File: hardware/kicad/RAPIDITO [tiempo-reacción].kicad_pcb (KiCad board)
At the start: 2 copper layers, 109.4 x 93.2 mm, 33 parts, among them J2 Screw_Terminal_01x19, J3 Screw_Terminal_01x19, Q1 2N3904

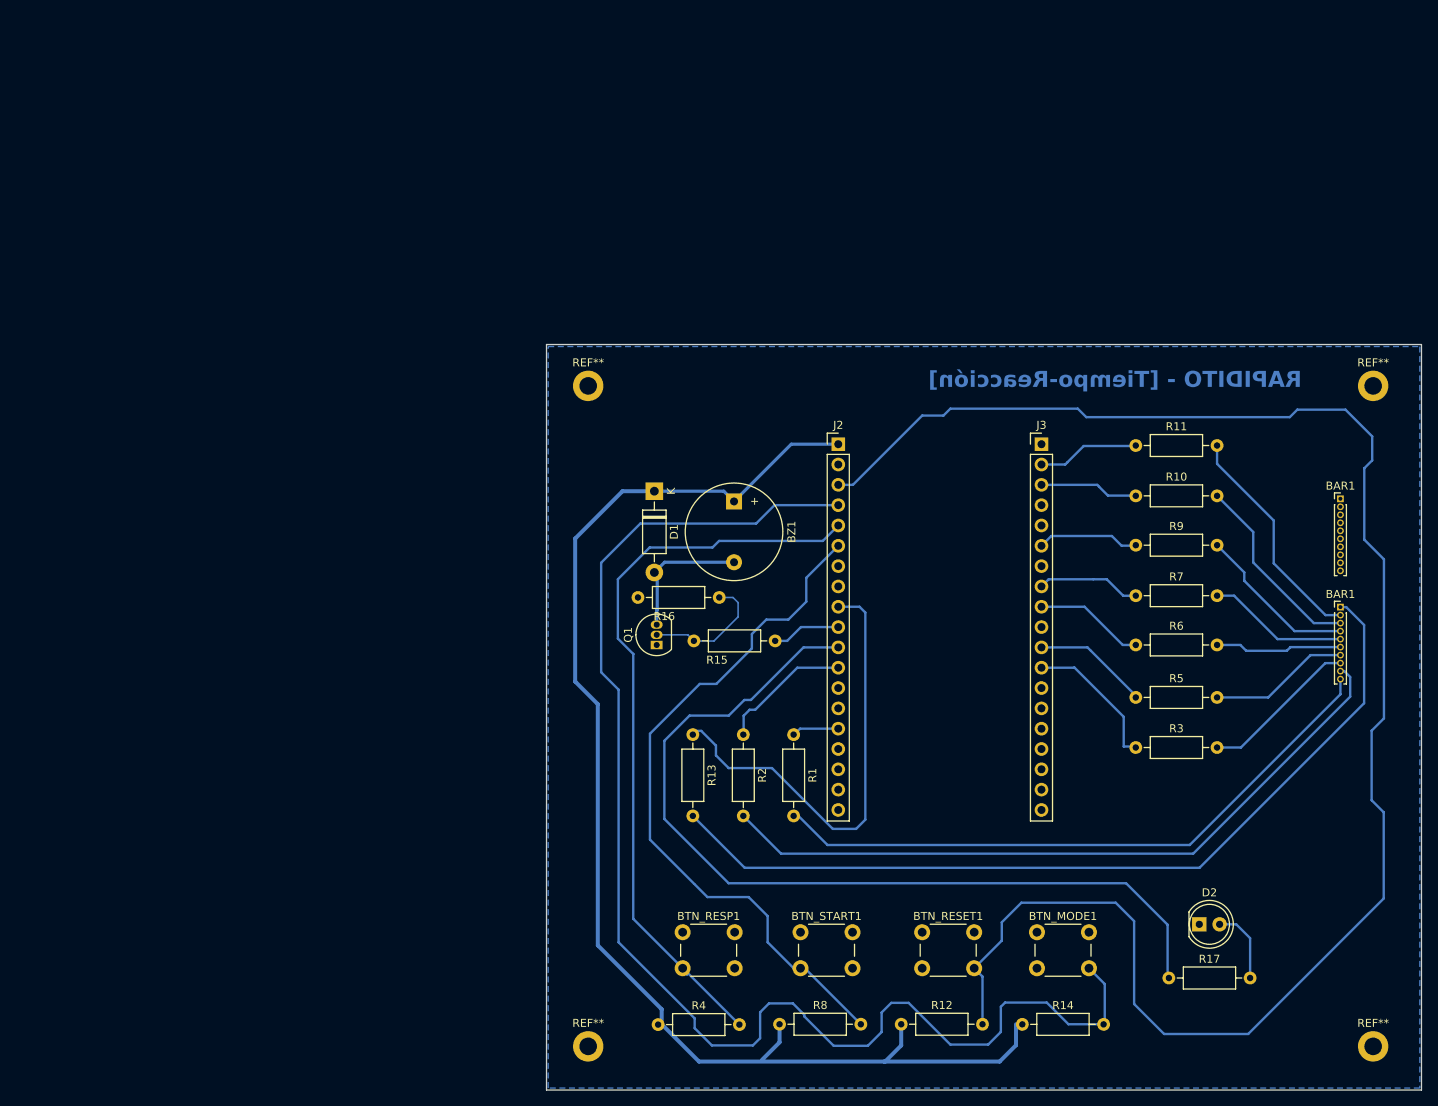
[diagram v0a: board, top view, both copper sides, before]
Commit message: KiCad v0.2: pinout ESP32 DevKit 30 pines, botones con pull-up interna, buzzer a 5 V, resistencias SMD, logo
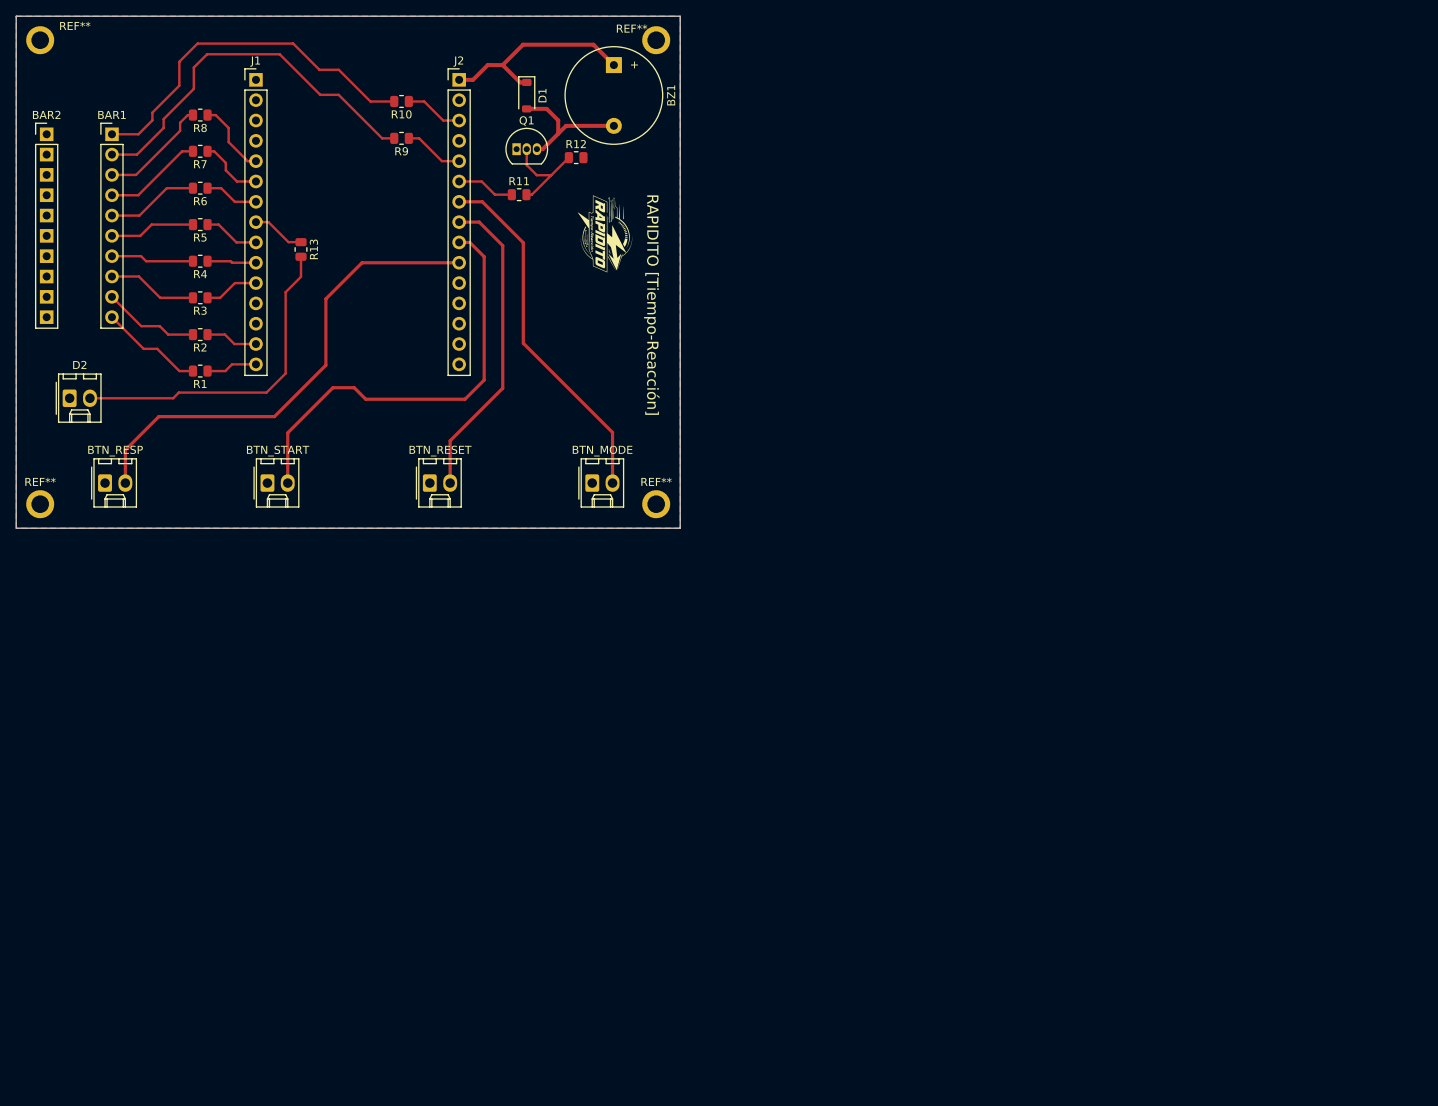
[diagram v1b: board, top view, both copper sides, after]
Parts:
- removed the BAR1 at (165.5, 73.9)
- removed the BAR1 at (165.5, 60.3)
- removed BTN_MODE1: PB4, Button_Switch_THT:SW_PUSH_6mm
- removed BTN_RESET1: PB3, Button_Switch_THT:SW_PUSH_6mm
- removed BTN_RESP1: PB1, Button_Switch_THT:SW_PUSH_6mm
- removed BTN_START1: PB2, Button_Switch_THT:SW_PUSH_6mm
- removed J3: Screw_Terminal_01x19, Connector_PinHeader_2.54mm:PinHeader_1x19_P2.54mm_Vertical
- removed R14, R16: 10kΩ, Resistor_THT:R_Axial_DIN0207_L6.3mm_D2.5mm_P10.16mm_Horizontal
- removed R15: 1kΩ, Resistor_THT:R_Axial_DIN0207_L6.3mm_D2.5mm_P10.16mm_Horizontal
- removed R17: 330Ω, Resistor_THT:R_Axial_DIN0207_L6.3mm_D2.5mm_P10.16mm_Horizontal
- removed the REF** at (169.6, 128.8)
- removed the REF** at (71.5, 128.8)
- removed the REF** at (71.5, 46.2)
- removed the REF** at (169.6, 46.2)
- added BAR1: HDSP-4830_2, Connector_PinHeader_2.54mm:PinHeader_1x10_P2.54mm_Vertical, F.Cu at (12.0, 14.8)
- added BAR2: HDSP-4830_2, Connector_PinHeader_2.54mm:PinHeader_1x10_P2.54mm_Vertical, F.Cu at (3.81, 14.8)
- added BTN_MODE: PB4, Connector_Molex:Molex_KK-254_AE-6410-02A_1x02_P2.54mm_Vertical, F.Cu at (72.0, 58.4)
- added BTN_RESET: PB3, Connector_Molex:Molex_KK-254_AE-6410-02A_1x02_P2.54mm_Vertical, F.Cu at (51.7, 58.4)
- added BTN_RESP: PB1, Connector_Molex:Molex_KK-254_AE-6410-02A_1x02_P2.54mm_Vertical, F.Cu at (11.1, 58.4)
- added BTN_START: PB2, Connector_Molex:Molex_KK-254_AE-6410-02A_1x02_P2.54mm_Vertical, F.Cu at (31.4, 58.4)
- added G***: LOGO, Logo RAPIDITO [tiempo-reacción]:Logo Rapidito negativo 85, F.Cu at (73.6, 27.2)
- added J1: Screw_Terminal_01x15, Connector_PinHeader_2.54mm:PinHeader_1x15_P2.54mm_Vertical, F.Cu at (30.0, 7.96)
- added REF**: MountingHole_2.2mm_M2_ISO7380_Pad, MountingHole:MountingHole_2.2mm_M2_ISO7380_Pad, F.Cu at (3.00, 61.0)
- added REF**: MountingHole_2.2mm_M2_ISO7380_Pad, MountingHole:MountingHole_2.2mm_M2_ISO7380_Pad, F.Cu at (80.0, 61.0)
- added REF**: MountingHole_2.2mm_M2_ISO7380_Pad, MountingHole:MountingHole_2.2mm_M2_ISO7380_Pad, F.Cu at (3.00, 3.00)
- added REF**: MountingHole_2.2mm_M2_ISO7380_Pad, MountingHole:MountingHole_2.2mm_M2_ISO7380_Pad, F.Cu at (80.0, 3.00)
- D1: footprint Diode_THT:D_DO-41_SOD81_P10.16mm_Horizontal -> Diode_SMD:D_SOD-123
- D2: footprint LED_THT:LED_D5.0mm -> Connector_Molex:Molex_KK-254_AE-6410-02A_1x02_P2.54mm_Vertical
- J2: value Screw_Terminal_01x19 -> Screw_Terminal_01x15; footprint Connector_PinHeader_2.54mm:PinHeader_1x19_P2.54mm_Vertical -> Connector_PinHeader_2.54mm:PinHeader_1x15_P2.54mm_Vertical
- R1, R10, R12, R13, R2, R3, R5, R6, R7, R9: footprint Resistor_THT:R_Axial_DIN0207_L6.3mm_D2.5mm_P10.16mm_Horizontal -> Resistor_SMD:R_0805_2012Metric
- R11: value 330Ω -> 1kΩ; footprint Resistor_THT:R_Axial_DIN0207_L6.3mm_D2.5mm_P10.16mm_Horizontal -> Resistor_SMD:R_0805_2012Metric
- R4, R8: value 10kΩ -> 330Ω; footprint Resistor_THT:R_Axial_DIN0207_L6.3mm_D2.5mm_P10.16mm_Horizontal -> Resistor_SMD:R_0805_2012Metric
- moved D2 155.8 mm to (6.68, 47.8)
- moved R8 134.8 mm to (23.0, 12.4), turned to 180 degrees
- moved R5 131.0 mm to (23.0, 26.1), turned to 180 degrees
- moved R6 130.1 mm to (23.0, 21.5), turned to 180 degrees
- moved R3 129.8 mm to (23.0, 35.2), turned to 180 degrees
- moved R7 129.5 mm to (23.0, 16.9), turned to 180 degrees
- moved R12 115.7 mm to (70.0, 17.7)
- moved R4 111.3 mm to (23.0, 30.6), turned to 180 degrees
- moved R9 104.9 mm to (48.2, 15.3), turned to 180 degrees
- moved R10 104.2 mm to (48.2, 10.7), turned to 180 degrees
- moved R1 87.0 mm to (23.0, 44.4), turned to 180 degrees
- moved R2 84.3 mm to (23.0, 39.8), turned to 180 degrees
- moved R11 83.2 mm to (62.9, 22.3)
- moved R13 78.0 mm to (35.6, 29.2)
- moved J2 65.7 mm to (55.4, 7.96)
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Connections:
- BZ1 pad 1: VCC_3V3 -> VCC_5V
- D1 pad 1: VCC_3V3 -> VCC_5V
- J2 pad 1: VCC_3V3 -> VCC_5V
- J2 pad 10: BUZZER -> RESP_input
- J2 pad 11: LED_MODE -> unconnected-(J2-Pin_11-Pad11)
- J2 pad 12: LED2 -> unconnected-(J2-Pin_12-Pad12)
- J2 pad 14: GND -> unconnected-(J2-Pin_14-Pad14)
- J2 pad 15: LED1 -> unconnected-(J2-Pin_15-Pad15)
- J2 pad 2: unconnected-(J2-Pin_2-Pad2) -> GND
- J2 pad 3: RESET_input -> LED10
- J2 pad 4: MODE_input -> unconnected-(J2-Pin_4-Pad4)
- J2 pad 5: RESP_input -> LED9
- J2 pad 6: START_input -> BUZZER
- J2 pad 7: unconnected-(J2-Pin_7-Pad7) -> MODE_input
- J2 pad 8: unconnected-(J2-Pin_8-Pad8) -> RESET_input
- J2 pad 9: LED10 -> START_input
- R1 pad 1: Net-(J1-Pin_10) -> LED1
- R10 pad 1: Net-(J1-Pin_3) -> LED10
- R11 pad 1: Net-(J1-Pin_2) -> BUZZER
- R11 pad 2: Net-(BAR1-A-Pad2) (its old number) -> Net-(Q1-B)
- R12 pad 1: VCC_3V3 -> Net-(Q1-B)
- R12 pad 2: RESET_input -> GND
- R13 pad 1: Net-(J1-Pin_1) -> LED_MODE
- R13 pad 2: Net-(BAR1-A-Pad1) (its old number) -> Net-(D2-A)
- R2 pad 1: Net-(J1-Pin_9) -> LED2
- R3 pad 1: Net-(J1-Pin_8) -> LED3
- R4 pad 1: VCC_3V3 -> LED4
- R4 pad 2: RESP_input -> Net-(BAR1-A-Pad7)
- R5 pad 1: Net-(J1-Pin_7) -> LED5
- R6 pad 1: Net-(J1-Pin_6) -> LED6
- R7 pad 1: Net-(J1-Pin_5) -> LED7
- R8 pad 1: VCC_3V3 -> LED8
- R8 pad 2: START_input -> Net-(BAR1-A-Pad3)
- R9 pad 1: Net-(J1-Pin_4) -> LED9
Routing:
- net RESET_input: track 217.1 -> 39.1 mm
- net VCC_3V3: track 164.7 -> 0.00 mm
- net MODE_input: track 173.5 -> 44.8 mm
- net Net-(BAR1-A-Pad1) (its old number): track 108.8 -> 0.00 mm
- net LED_MODE: track 111.6 -> 6.67 mm
- net Net-(BAR1-A-Pad9): track 89.9 -> 12.1 mm
- net Net-(BAR1-A-Pad10): track 79.6 -> 12.9 mm
- net LED10: track 57.5 -> 7.28 mm
- net RESP_input: track 94.5 -> 60.4 mm
- net START_input: track 87.0 -> 54.0 mm
- net Net-(D2-A): track 9.51 -> 41.1 mm
- net Net-(BAR1-A-Pad2) (its old number): track 28.7 -> 0.00 mm
- net Net-(BAR1-A-Pad2): track 20.5 -> 47.0 mm
- net VCC_5V: track 0.00 -> 26.1 mm
- net Net-(BAR1-A-Pad1): track 24.2 -> 45.3 mm
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- added copper zone on F.Cu, net GND
- removed copper zone on B.Cu, net GND
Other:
- board size 109.4 x 93.2 mm -> 83 x 64 mm
- board text added: "RAPIDITO [Tiempo-Reacción]"
- board text removed: "RAPIDITO - [Tiempo-Reacción]"
